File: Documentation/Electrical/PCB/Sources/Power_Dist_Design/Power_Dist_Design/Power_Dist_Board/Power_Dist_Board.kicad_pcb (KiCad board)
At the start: 2 copper layers, 150.5 x 85 mm, 66 parts, among them J1 Battery Connector, J10 GND_Bridge_3, J2 +5V, J3 +5V, J4 +3.3V, J5 +3.3V, J6 GND, J7 GND, J8 GND_Bridge_1, J9 GND_Bridge_2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

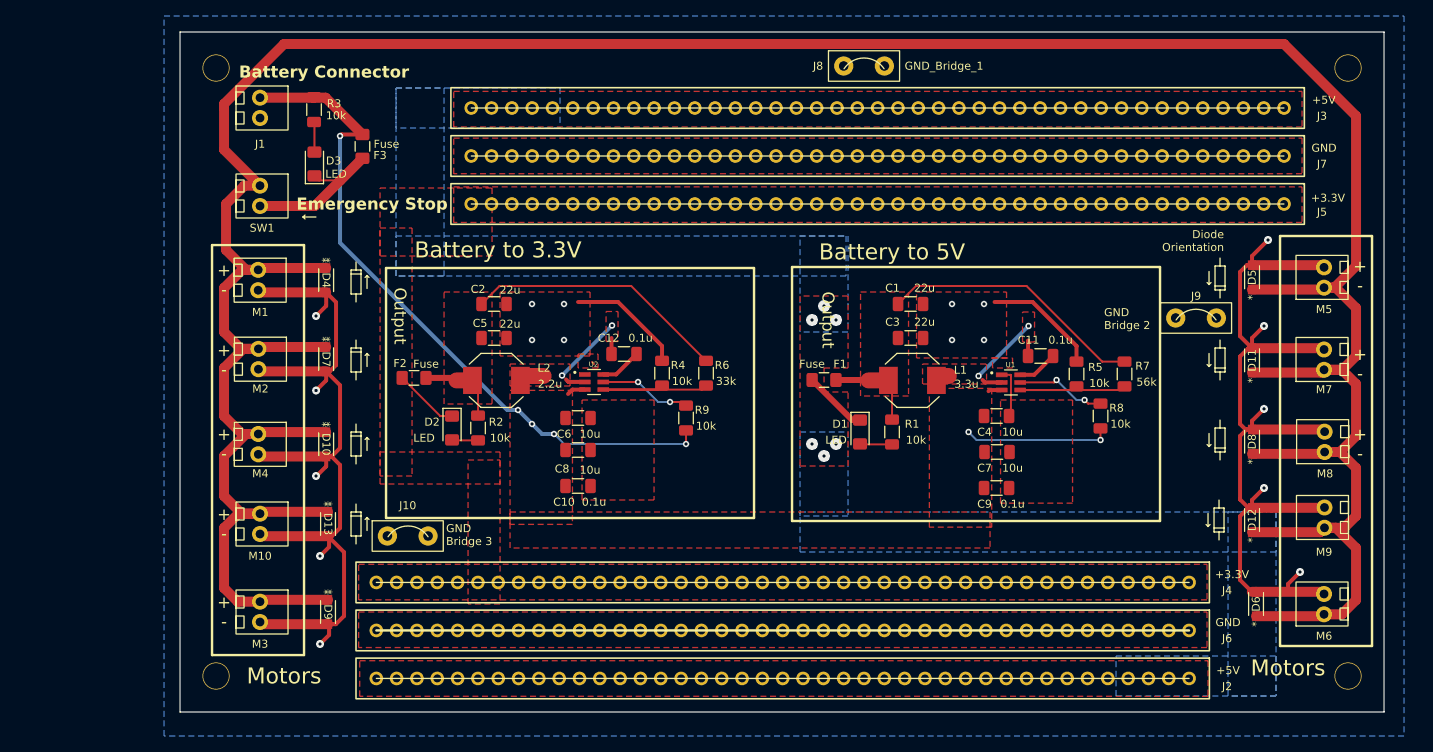
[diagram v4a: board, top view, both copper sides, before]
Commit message: Reduced length by 5mm to fit in chassis
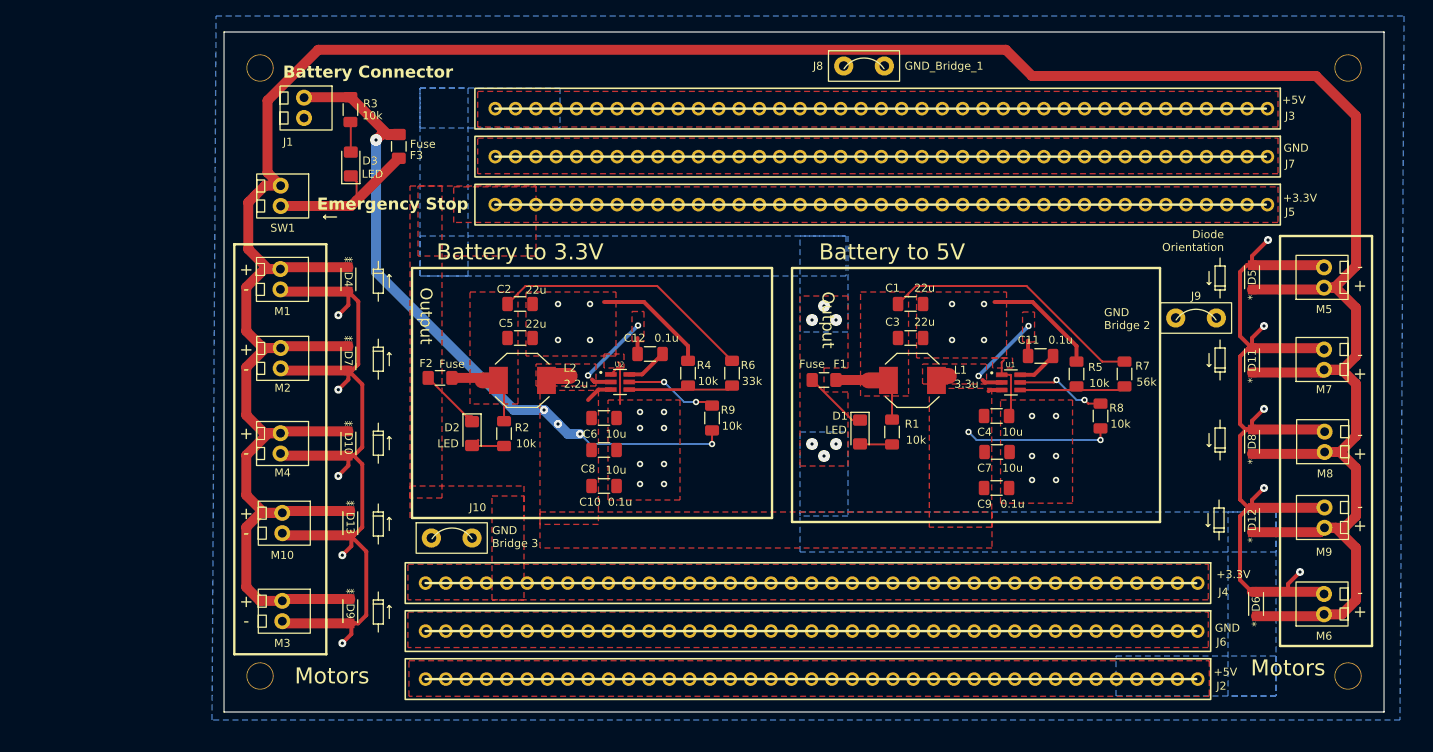
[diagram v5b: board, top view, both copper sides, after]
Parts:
- moved J10 5.51 mm to (116.0, 82.8)
- moved J1 5.50 mm to (97.5, 29.0)
- moved REF** 5.50 mm to (92.0, 100.0)
- moved REF** 5.50 mm to (92.0, 24.0)
- moved D3 4.55 mm to (103.3, 36.0)
- moved F3 4.55 mm to (109.3, 33.8)
- moved R3 4.55 mm to (103.3, 29.2)
- moved R2 3.32 mm to (122.5, 69.7)
- moved C10 3.25 mm to (135.0, 76.2)
- moved C12 3.25 mm to (140.8, 59.8)
- moved C2 3.25 mm to (124.5, 53.5)
- moved C5 3.25 mm to (124.5, 57.8)
- moved C6 3.25 mm to (135.0, 67.8)
- moved C8 3.25 mm to (135.0, 71.8)
- moved F2 3.25 mm to (114.5, 62.7)
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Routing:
- net GND: track 251.4 -> 260.3 mm, vias 18 -> 32
- net +12V: track 416.1 -> 408.9 mm
- net Net-(D3-K): track 18.7 -> 20.6 mm
- net +3.3V: track 8.22 -> 7.47 mm
- net /vin: track 108.8 -> 109.5 mm
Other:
- board size 150.5 x 85 mm -> 145 x 85 mm
- board text added: "- +"

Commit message: Added to wireless charging signoff
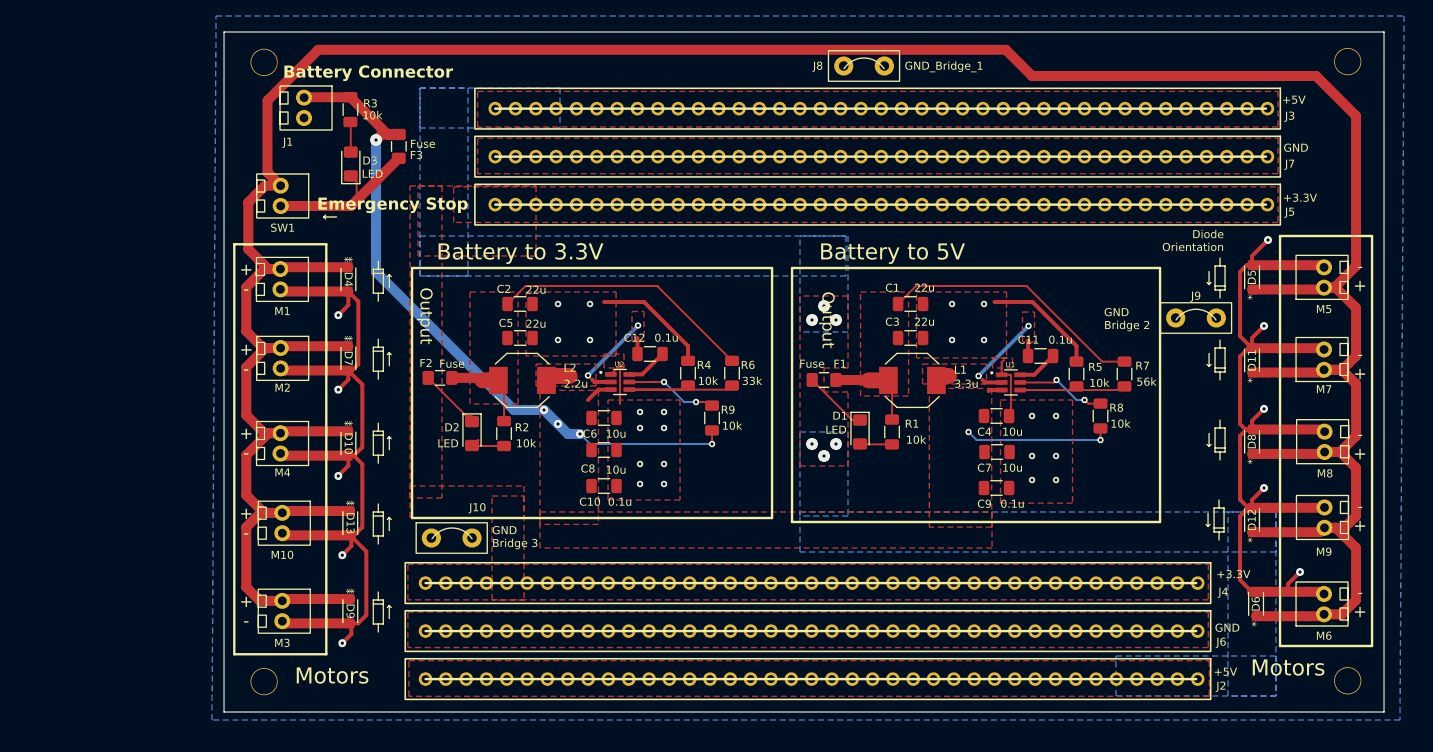
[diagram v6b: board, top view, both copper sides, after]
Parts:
- moved REF** 0.87 mm to (92.5, 100.7)
- moved REF** 0.87 mm to (92.5, 23.3)
- moved REF** 0.80 mm to (228.0, 23.2)
- moved REF** 0.60 mm to (228.0, 100.6)
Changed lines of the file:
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@@
   (net 19 "Net-(D3-A)")
   (footprint "MountingHole:MountingHole_3.2mm_M3_DIN965" (layer "F.Cu")
-    (at 228 100)
+    (at 227.96 100.6)
     (descr "Mounting Hole 3.2mm, no annular, M3, DIN965")
     (tags "mounting hole 3.2mm no annular m3 din965")
@@
   )
   (footprint "MountingHole:MountingHole_3.2mm_M3_DIN965" (layer "F.Cu")
-    (at 92 100)
+    (at 92.51 100.7)
     (descr "Mounting Hole 3.2mm, no annular, M3, DIN965")
     (tags "mounting hole 3.2mm no annular m3 din965")
@@
         (effects (font (size 1 1) (thickness 0.15)))
     )
-    (fp_text user "${REFERENCE}" (at 0 0) (layer "F.Fab")
-        (effects (font (size 1 1) (thickness 0.15)))
-    )
     (fp_circle (center 0 0) (end 2.8 0)
       (stroke (width 0.15) (type solid)) (fill none) (layer "Cmts.User"))
@@
   )
   (footprint "MountingHole:MountingHole_3.2mm_M3_DIN965" (layer "F.Cu")
-    (at 228 24)
+    (at 227.96 23.2)
     (descr "Mounting Hole 3.2mm, no annular, M3, DIN965")
     (tags "mounting hole 3.2mm no annular m3 din965")
@@
   )
   (footprint "MountingHole:MountingHole_3.2mm_M3_DIN965" (layer "F.Cu")
-    (at 92 24)
+    (at 92.51 23.3)
     (descr "Mounting Hole 3.2mm, no annular, M3, DIN965")
     (tags "mounting hole 3.2mm no annular m3 din965")
@@
   )
   (dimension (type aligned) (layer "Eco1.User")
+    (pts (xy 227.96 100.6) (xy 227.96 23.2))
+    (height 12.94)
+    (gr_text "77.4000 mm" (at 239.75 61.9 90) (layer "Eco1.User")
+      (effects (font (size 1 1) (thickness 0.15)))
+    )
+    (format (prefix "") (suffix "") (units 3) (units_format 1) (precision 4))
+    (style (thickness 0.15) (arrow_length 1.27) (text_position_mode 0) (extension_height 0.58642) (extension_offset 0.5) keep_text_aligned)
+  )
+  (dimension (type aligned) (layer "Eco1.User")
+    (pts (xy 92.51 100.7) (xy 227.96 100.6))
+    (height 9.699626)
+    (gr_text "135.4500 mm" (at 160.241312 109.199623 0.04230030942) (layer "Eco1.User")
+      (effects (font (size 1 1) (thickness 0.15)))
+    )
+    (format (prefix "") (suffix "") (units 3) (units_format 1) (precision 4))
+    (style (thickness 0.15) (arrow_length 1.27) (text_position_mode 0) (extension_height 0.58642) (extension_offset 0.5) keep_text_aligned)
+  )
+  (dimension (type aligned) (layer "Eco1.User")
     (pts (xy 87.5 104.5) (xy 232.5 104.5))
     (height 12.75)
@@
       (effects (font (size 1 1) (thickness 0.15)))
     )
+    (format (prefix "") (suffix "") (units 3) (units_format 1) (precision 4))
+    (style (thickness 0.15) (arrow_length 1.27) (text_position_mode 0) (extension_height 0.58642) (extension_offset 0.5) keep_text_aligned)
+  )
+  (dimension (type aligned) (layer "Eco1.User")
+    (pts (xy 227.96 23.2) (xy 92.51 23.3))
+    (height 9.699626)
+    (gr_text "135.4500 mm" (at 160.22699 12.400377 0.04230030942) (layer "Eco1.User")
+      (effects (font (size 1 1) (thickness 0.15)))
+    )
+    (format (prefix "") (suffix "") (units 3) (units_format 1) (precision 4))
+    (style (thickness 0.15) (arrow_length 1.27) (text_position_mode 0) (extension_height 0.58642) (extension_offset 0.5) keep_text_aligned)
+  )
+  (dimension (type aligned) (layer "Eco1.User")
+    (pts (xy 92 23.3) (xy 92 100.7))
+    (height 12.94)
+    (gr_text "77.4000 mm" (at 77.91 62 90) (layer "Eco1.User")
+      (effects (font (size 1 1) (thickness 0.15)))
+    )
